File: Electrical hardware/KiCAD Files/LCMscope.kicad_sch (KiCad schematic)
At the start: 0 parts

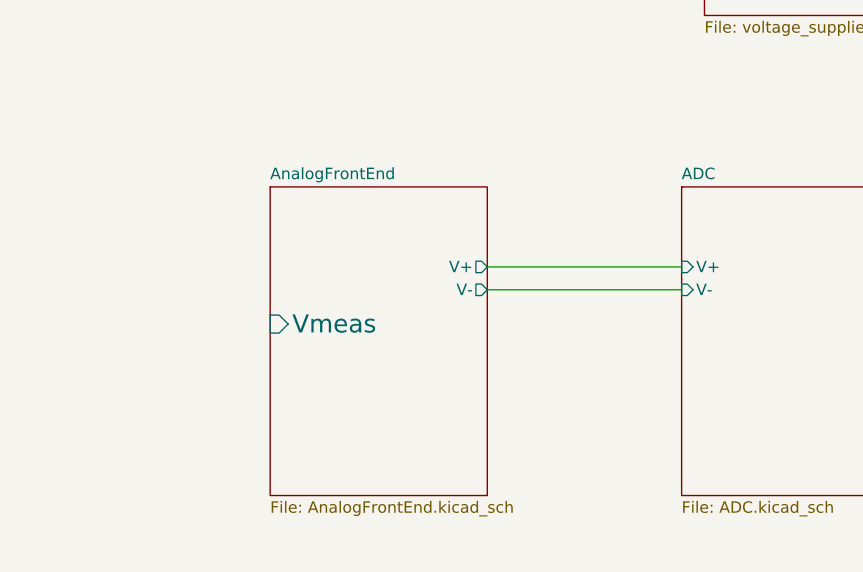
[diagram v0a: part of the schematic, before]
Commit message: adding voltage divider
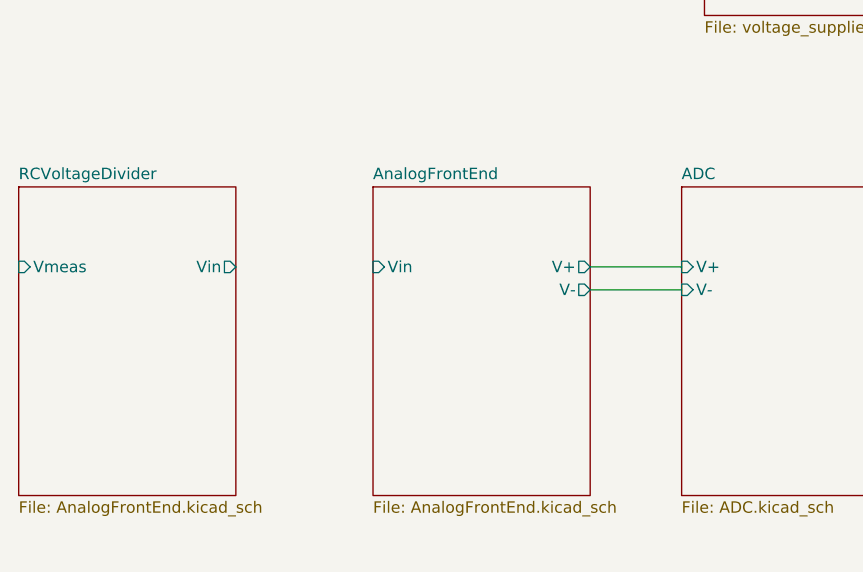
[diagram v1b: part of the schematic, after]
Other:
- added sheet RCVoltageDivider (AnalogFrontEnd.kicad_sch)
- sheet AnalogFrontEnd ports: added Vin; removed Vmeas
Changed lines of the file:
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@@
 	(wire
 		(pts
-			(xy 81.28 68.58) (xy 102.87 68.58)
+			(xy 92.71 68.58) (xy 102.87 68.58)
 		)
 		(stroke
@@
 	(wire
 		(pts
-			(xy 81.28 71.12) (xy 102.87 71.12)
+			(xy 92.71 71.12) (xy 102.87 71.12)
 		)
 		(stroke
@@
 	)
 	(sheet
-		(at 57.15 59.69)
+		(at 68.58 59.69)
 		(size 24.13 34.29)
 		(exclude_from_sim no)
@@
 		)
 		(property "Sheetname" "AnalogFrontEnd"
-			(at 57.15 58.9784 0)
+			(at 68.58 58.9784 0)
 			(effects
 				(font
@@
 		)
 		(property "Sheetfile" "AnalogFrontEnd.kicad_sch"
-			(at 57.15 94.5646 0)
+			(at 68.58 94.5646 0)
 			(effects
 				(font
@@
 		)
 		(pin "V+" output
-			(at 81.28 68.58 0)
+			(at 92.71 68.58 0)
 			(effects
 				(font
@@
 		)
 		(pin "V-" output
-			(at 81.28 71.12 0)
-			(effects
-				(font
-					(size 1.27 1.27)
-				)
-				(justify right)
-			)
-		)
-		(pin "Vmeas" input
-			(at 57.15 74.93 180)
-			(effects
-				(font
-					(size 2 2)
+			(at 92.71 71.12 0)
+			(effects
+				(font
+					(size 1.27 1.27)
+				)
+				(justify right)
+			)
+		)
+		(pin "Vin" input
+			(at 68.58 68.58 180)
+			(effects
+				(font
+					(size 1.27 1.27)
 				)
 				(justify left)
@@
 				)
 			)
+		)
+	)
+	(sheet
+		(at 29.21 59.69)
+		(size 24.13 34.29)
+		(exclude_from_sim no)
+		(in_bom yes)
+		(on_board yes)
+		(dnp no)
+		(fields_autoplaced yes)
+		(stroke
+			(width 0.1524)
+			(type solid)
+		)
+		(fill
+			(color 255 194 1 1.0000)
+		)
+		(property "Sheetname" "RCVoltageDivider"
+			(at 29.21 58.9784 0)
+			(effects
+				(font
+					(size 1.27 1.27)
+				)
+				(justify left bottom)
+			)
+		)
+		(property "Sheetfile" "AnalogFrontEnd.kicad_sch"
+			(at 29.21 94.5646 0)
+			(effects
+				(font
+					(size 1.27 1.27)
+				)
+				(justify left top)
+			)
+		)
+		(pin "Vin" output
+			(at 53.34 68.58 0)
+			(effects
+				(font
+					(size 1.27 1.27)
+				)
+				(justify right)
+			)
+		)
+		(pin "Vmeas" input
+			(at 29.21 68.58 180)
+			(effects
+				(font
+					(size 1.27 1.27)
+				)
+				(justify left)
+			)
+		)
+		(instances
+			(project "LCMscope"
+				(path "/6a8b9a9c-88ba-48a5-8033-e5e1453b50bb"
+					(page "6")
+				)
+			)
